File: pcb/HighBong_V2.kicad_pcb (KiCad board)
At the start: 2 copper layers, 24 x 55 mm, 18 parts, among them J1 LEDs, J2 Programming header, J3 Power, Q1 BC817, Q2 BC817, Q3 BC817, Q4 BC817, SW1 Bootloader, SW2 Mode Button, U1 AMS1117-3.3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

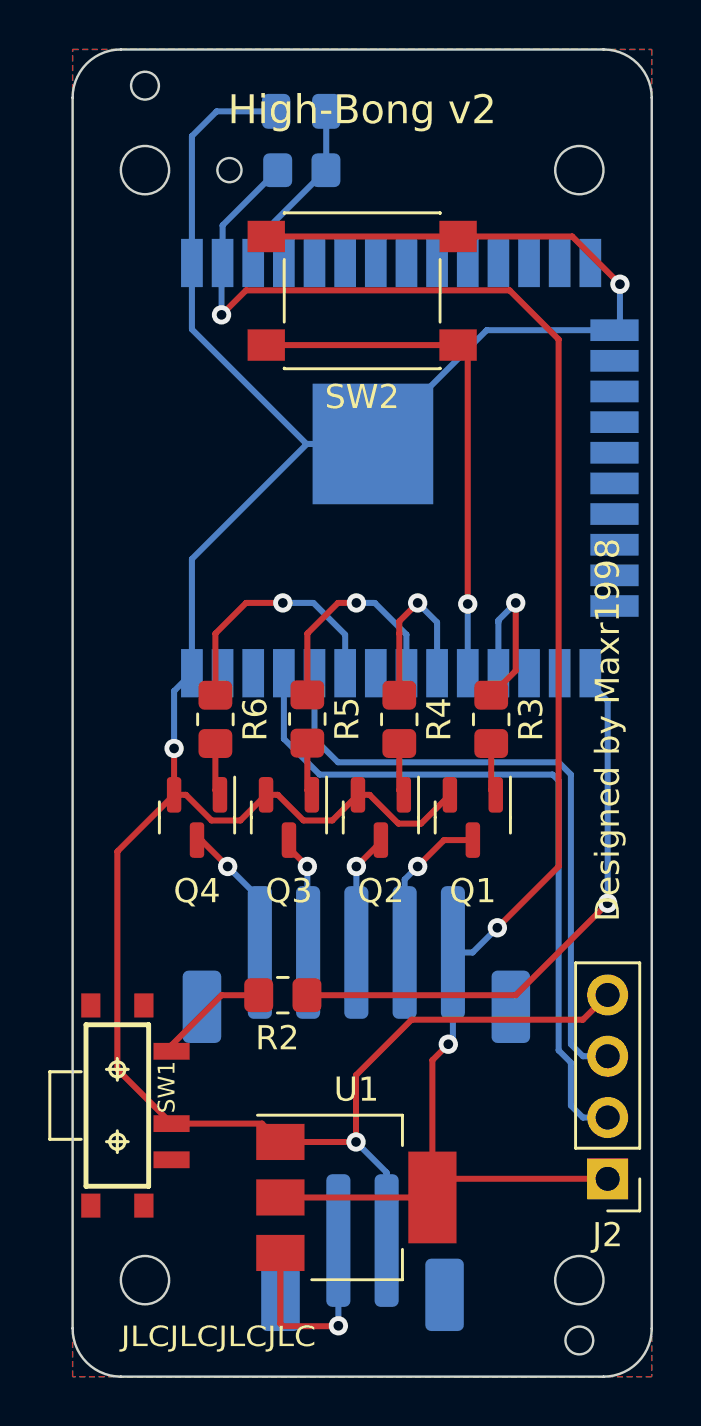
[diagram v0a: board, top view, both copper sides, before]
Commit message: Fix issues with drill holes and swtich footprint
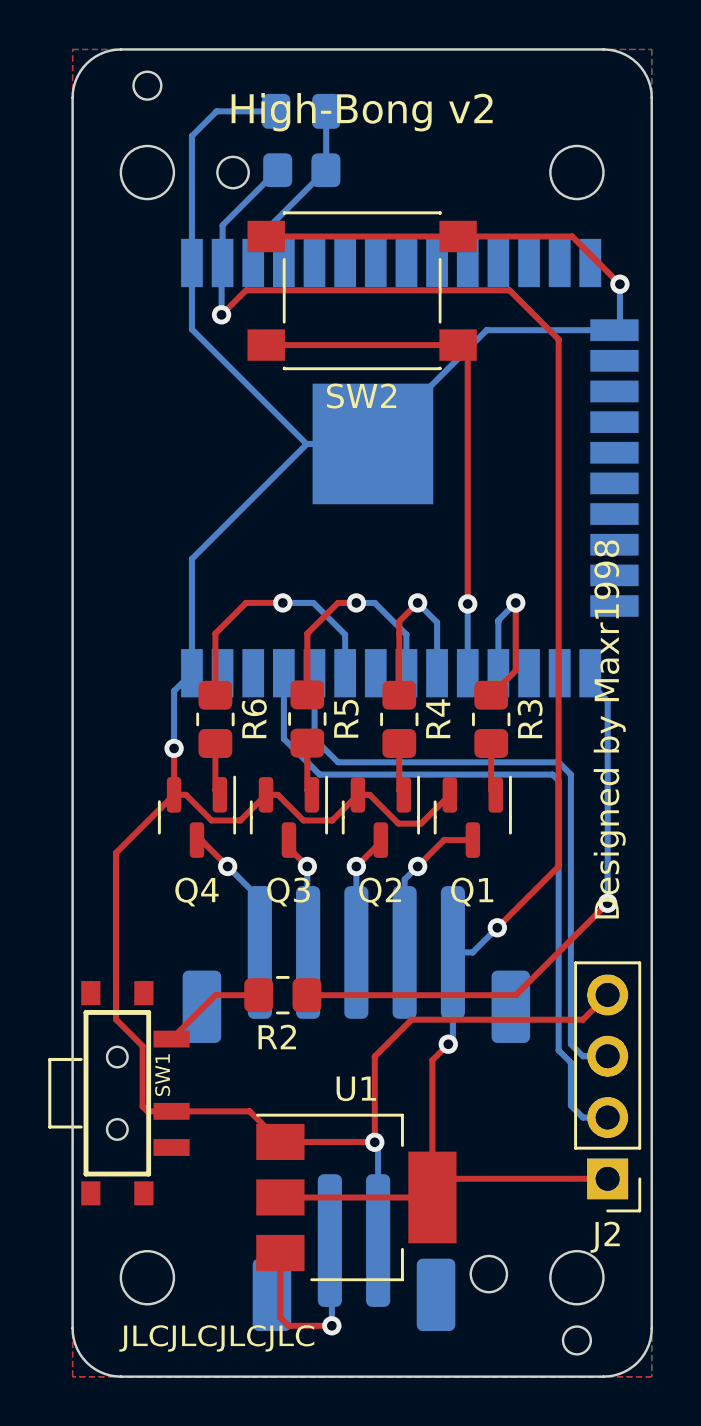
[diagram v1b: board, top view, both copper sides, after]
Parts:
- SW1: footprint footprints:KPS-1290 -> Custom:KPS-1290
- moved SW1 0.51 mm to (101.9, 143.3)
- moved J3 0.35 mm to (111.7, 149.9)
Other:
- outline, holes or cut-outs redrawn

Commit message: Move button to GPIO14
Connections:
- U2 pad 13: unconnected-(U2-Pad13) -> Net-(SW2-Pad1)
- U2 pad 29: Net-(SW2-Pad1) -> unconnected-(U2-Pad29)
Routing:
- net Net-(SW2-Pad1): track 21.7 -> 14.3 mm
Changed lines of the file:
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@@
   (net 18 "unconnected-(U2-Pad11)")
   (net 19 "unconnected-(U2-Pad12)")
-  (net 20 "unconnected-(U2-Pad13)")
+  (net 20 "unconnected-(U2-Pad29)")
   (net 21 "unconnected-(U2-Pad14)")
   (net 22 "unconnected-(U2-Pad16)")
@@
       (net 19 "unconnected-(U2-Pad12)") (pinfunction "IO27") (pintype "bidirectional+no_connect"))
     (pad "13" smd rect (at -8.5 -6.985 270) (size 2 0.9) (layers "B.Cu" "B.Paste" "B.Mask")
-      (net 20 "unconnected-(U2-Pad13)") (pinfunction "IO14") (pintype "bidirectional+no_connect"))
+      (net 44 "Net-(SW2-Pad1)") (pinfunction "IO14") (pintype "bidirectional"))
     (pad "14" smd rect (at -8.5 -8.255 270) (size 2 0.9) (layers "B.Cu" "B.Paste" "B.Mask")
       (net 21 "unconnected-(U2-Pad14)") (pinfunction "IO12") (pintype "bidirectional+no_connect"))
@@
       (net 6 "Net-(R3-Pad1)") (pinfunction "IO17") (pintype "bidirectional"))
     (pad "29" smd rect (at 8.5 -3.175 270) (size 2 0.9) (layers "B.Cu" "B.Paste" "B.Mask")
-      (net 44 "Net-(SW2-Pad1)") (pinfunction "IO5") (pintype "bidirectional"))
+      (net 20 "unconnected-(U2-Pad29)") (pinfunction "IO5") (pintype "bidirectional+no_connect"))
     (pad "30" smd rect (at 8.5 -1.905 270) (size 2 0.9) (layers "B.Cu" "B.Paste" "B.Mask")
       (net 9 "Net-(R4-Pad1)") (pinfunction "IO18") (pintype "bidirectional"))
@@
   (segment (start 122.682 111.406) (end 122.455 111.633) (width 0.25) (layer "B.Cu") (net 2))
   (segment (start 122.682 109.728) (end 122.682 111.406) (width 0.25) (layer "B.Cu") (net 2))
+  (segment (start 121.205 111.633) (end 116.49 116.348) (width 0.25) (layer "B.Cu") (net 2))
   (segment (start 104.945 103.589) (end 104.945 108.848) (width 0.25) (layer "B.Cu") (net 2))
   (segment (start 104.945 108.848) (end 104.945 111.598) (width 0.25) (layer "B.Cu") (net 2))
@@
   (segment (start 112.662 145.428) (end 112.522 145.288) (width 0.25) (layer "B.Cu") (net 2))
   (segment (start 109.712 116.348) (end 104.945 121.115) (width 0.25) (layer "B.Cu") (net 2))
-  (segment (start 112.445 116.348) (end 117.16 111.633) (width 0.25) (layer "B.Cu") (net 2))
-  (segment (start 117.16 111.633) (end 122.455 111.633) (width 0.25) (layer "B.Cu") (net 2))
+  (segment (start 116.49 116.348) (end 112.445 116.348) (width 0.25) (layer "B.Cu") (net 2))
+  (segment (start 122.455 111.633) (end 121.205 111.633) (width 0.25) (layer "B.Cu") (net 2))
   (segment (start 112.445 116.348) (end 109.712 116.348) (width 0.25) (layer "B.Cu") (net 2))
   (segment (start 120.65 130.048) (end 120.142 129.54) (width 0.25) (layer "B.Cu") (net 3))
@@
   (segment (start 105.918 128.762) (end 105.918 130.7005) (width 0.25) (layer "F.Cu") (net 43))
   (segment (start 108.025 112.25) (end 115.975 112.25) (width 0.25) (layer "F.Cu") (net 44))
-  (segment (start 116.375 122.979) (end 116.375 112.65) (width 0.25) (layer "F.Cu") (net 44))
-  (segment (start 116.375 112.65) (end 115.975 112.25) (width 0.25) (layer "F.Cu") (net 44))
-  (via (at 116.375 122.979) (size 0.8) (drill 0.4) (layers "F.Cu" "B.Cu") (net 44))
-  (segment (start 116.375 125.848) (end 116.375 122.979) (width 0.25) (layer "B.Cu") (net 44))
+  (segment (start 118.0404 112.2426) (end 115.9824 112.2426) (width 0.25) (layer "F.Cu") (net 44))
+  (segment (start 115.9824 112.2426) (end 115.975 112.25) (width 0.25) (layer "F.Cu") (net 44))
+  (via (at 118.0404 112.2426) (size 0.8) (drill 0.4) (layers "F.Cu" "B.Cu") (net 44))
+  (segment (start 120.185 110.098) (end 118.0404 112.2426) (width 0.25) (layer "B.Cu") (net 44))
+  (segment (start 120.185 108.848) (end 120.185 110.098) (width 0.25) (layer "B.Cu") (net 44))
   (segment (start 110.998 122.936) (end 111.76 122.936) (width 0.25) (layer "F.Cu") (net 45))
   (segment (start 109.728 124.206) (end 110.998 122.936) (width 0.25) (layer "F.Cu") (net 45))
